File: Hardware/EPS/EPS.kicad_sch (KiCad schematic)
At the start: 0 parts

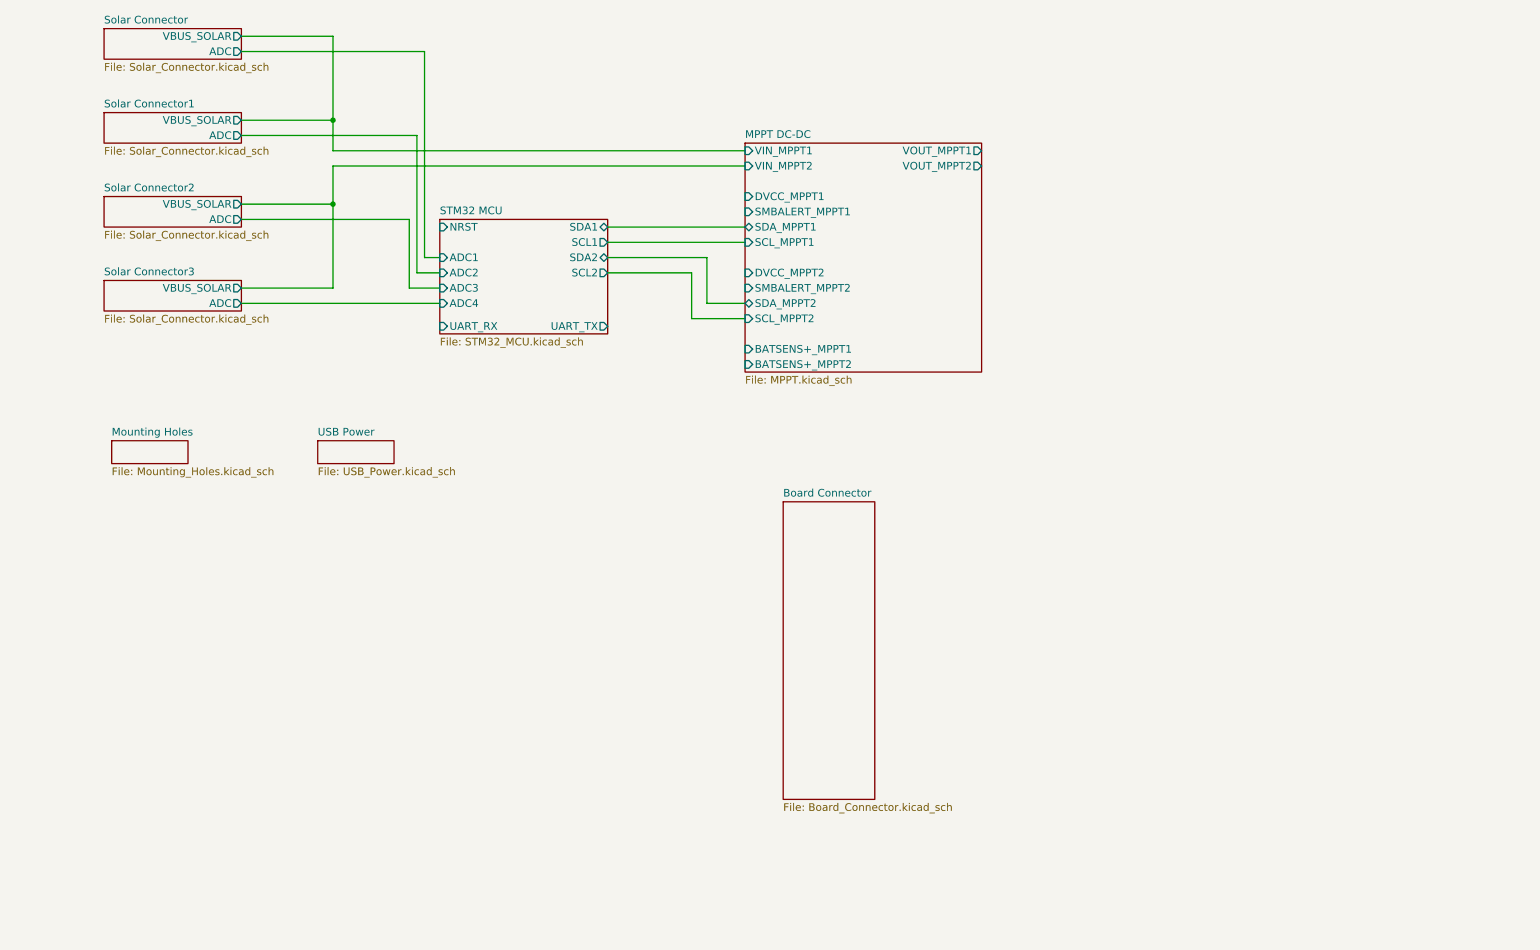
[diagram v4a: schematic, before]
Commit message: Added board connector layout
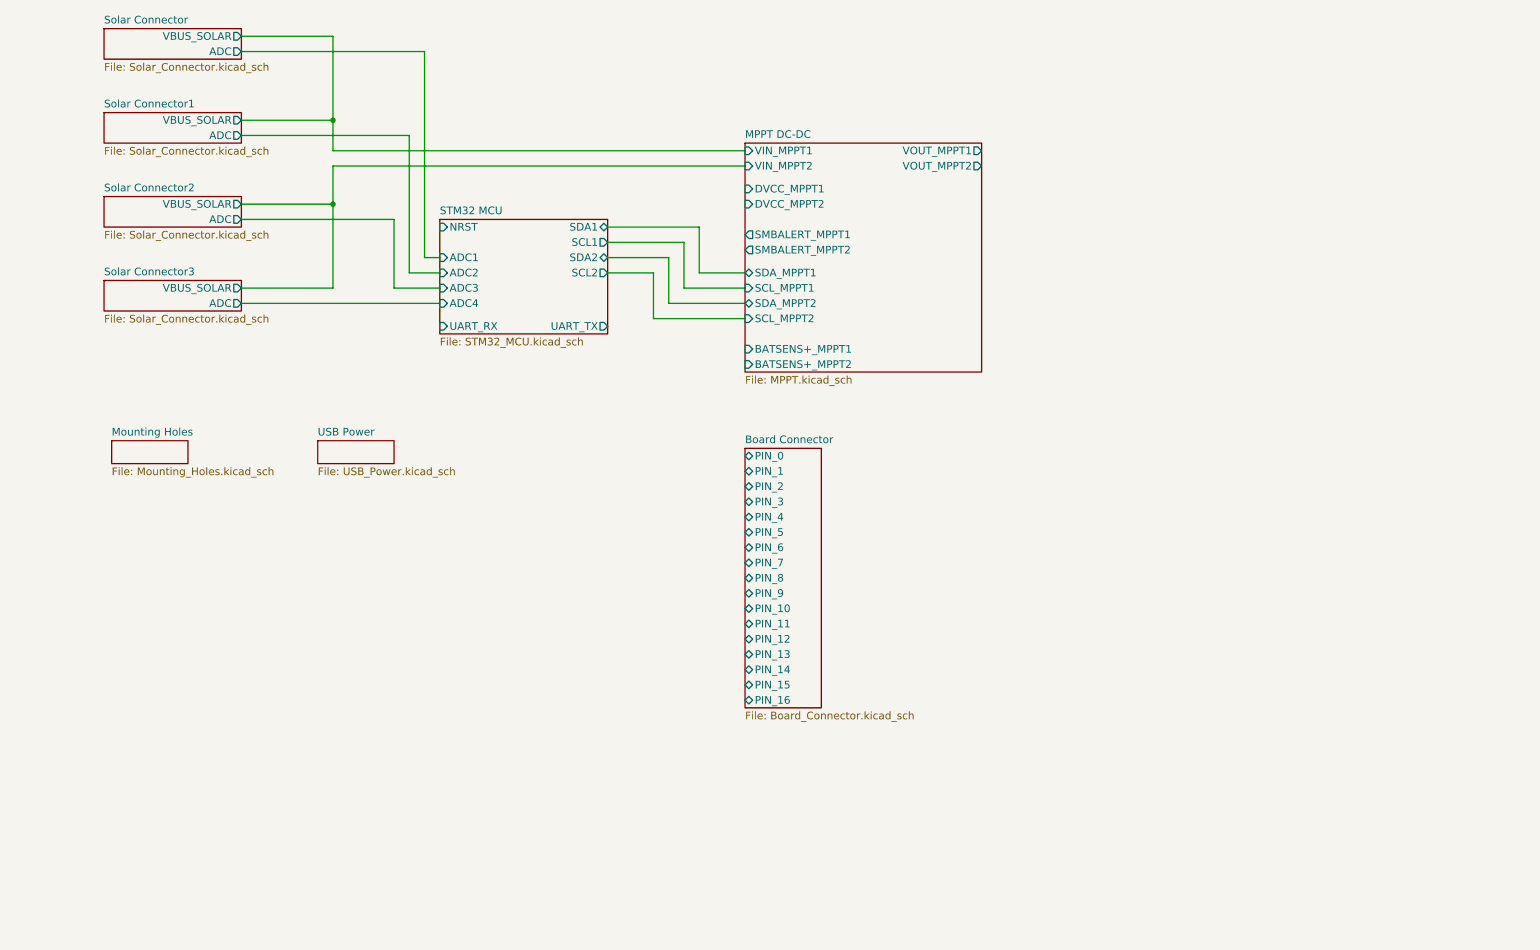
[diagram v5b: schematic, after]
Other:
- sheet Board Connector ports: added PIN_0, PIN_1, PIN_10, PIN_11, PIN_12, PIN_13, PIN_14, PIN_15, PIN_16, PIN_2, PIN_3, PIN_4, PIN_5, PIN_6, PIN_7, PIN_8, PIN_9; removed none

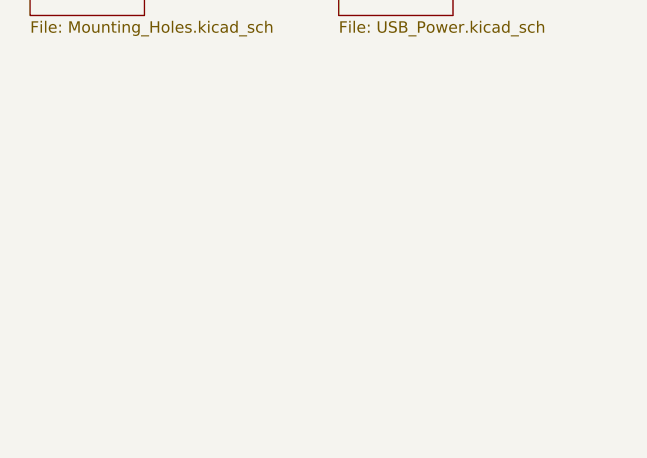
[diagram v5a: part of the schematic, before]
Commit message: Added Power sheet and ESD Protection
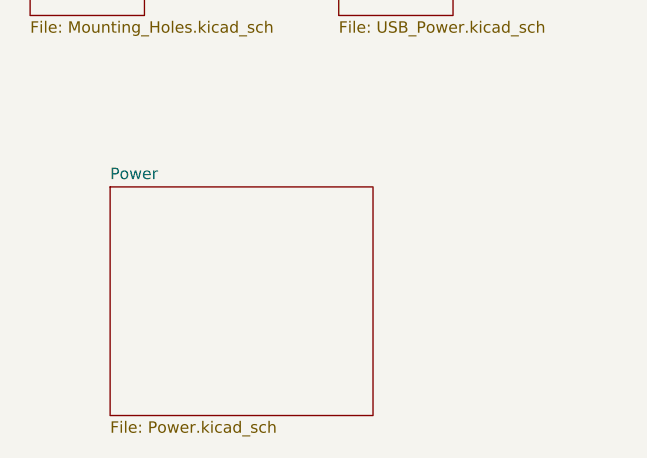
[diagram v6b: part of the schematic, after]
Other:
- added sheet Power (Power.kicad_sch)

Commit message: EPS v0.0.1
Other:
- removed sheet Solar Connector
- removed sheet Solar Connector1
- removed sheet Solar Connector2
- removed sheet Solar Connector3
- added sheet Battery_Connector (Battery_Connector.kicad_sch)
- added sheet Solar_Connector (Solar_Connector.kicad_sch)
- added sheet Solar_Connector1 (Solar_Connector.kicad_sch)
- added sheet Solar_Connector2 (Solar_Connector.kicad_sch)
- added sheet Solar_Connector3 (Solar_Connector.kicad_sch)
- sheet MPPT DC-DC ports: added ~{SMBALERT_MPPT1}; removed BATSENS+_MPPT2, DVCC_MPPT2, SCL_MPPT2, SDA_MPPT2, SMBALERT_MPPT1, SMBALERT_MPPT2, VIN_MPPT2, VOUT_MPPT2
- sheet Power ports: added EN_3V3, EN_5V0, VBUS_IN; removed none
- sheet STM32 MCU ports: added none; removed SCL2, SDA2
- sheet USB Power ports: added USB_VBUS; removed none

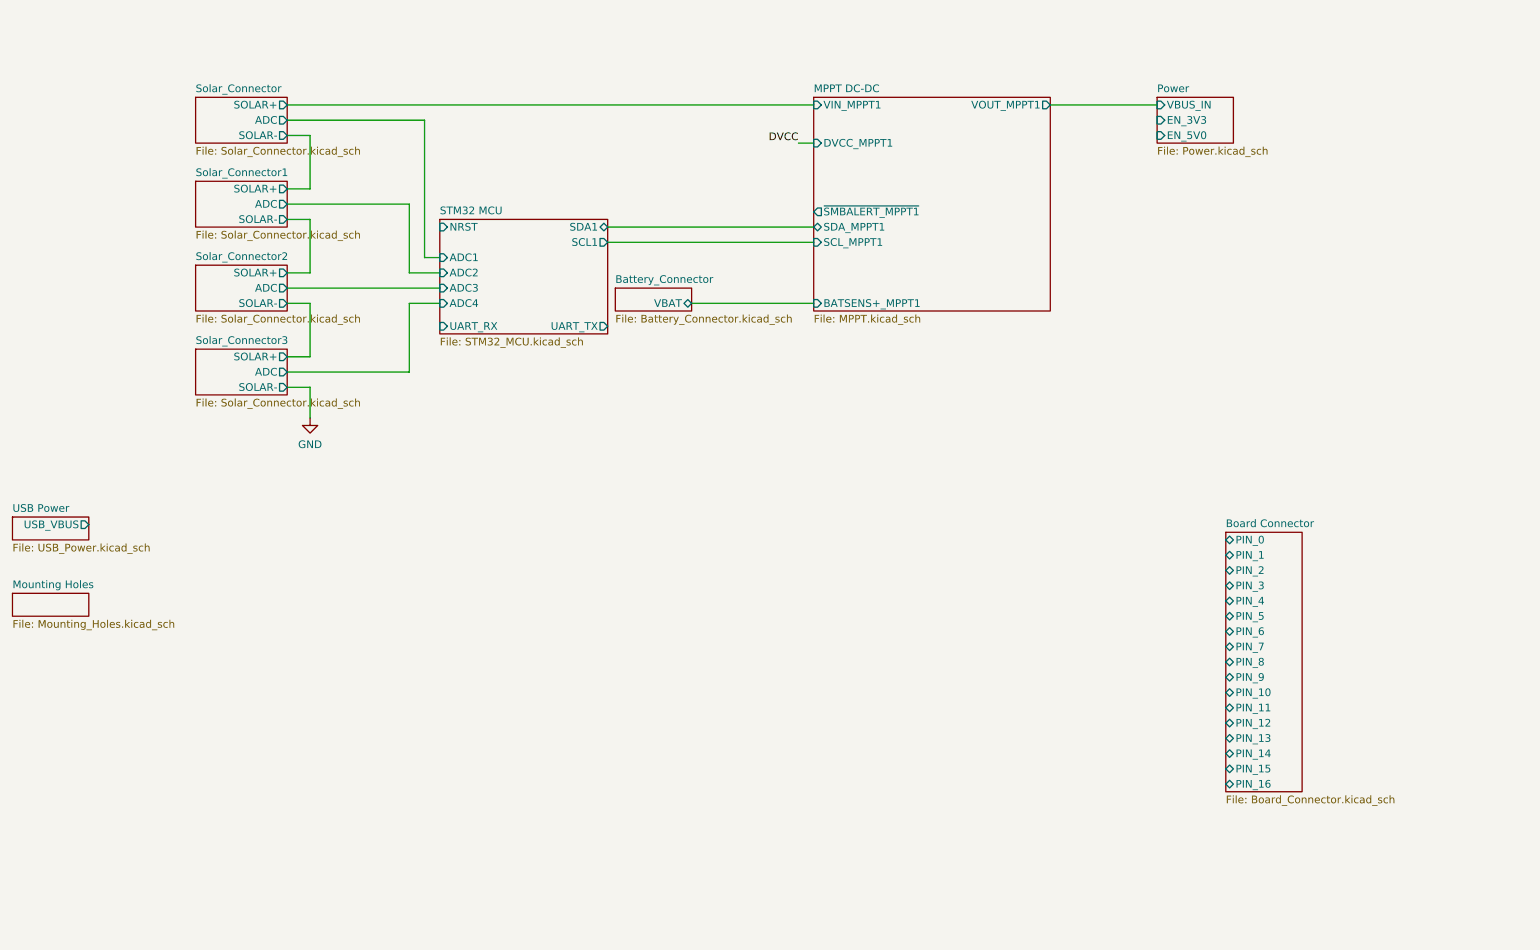
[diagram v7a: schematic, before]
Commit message: Fuse, Power Switch to 3.3V, connector ESD Prot.
v0.0.2
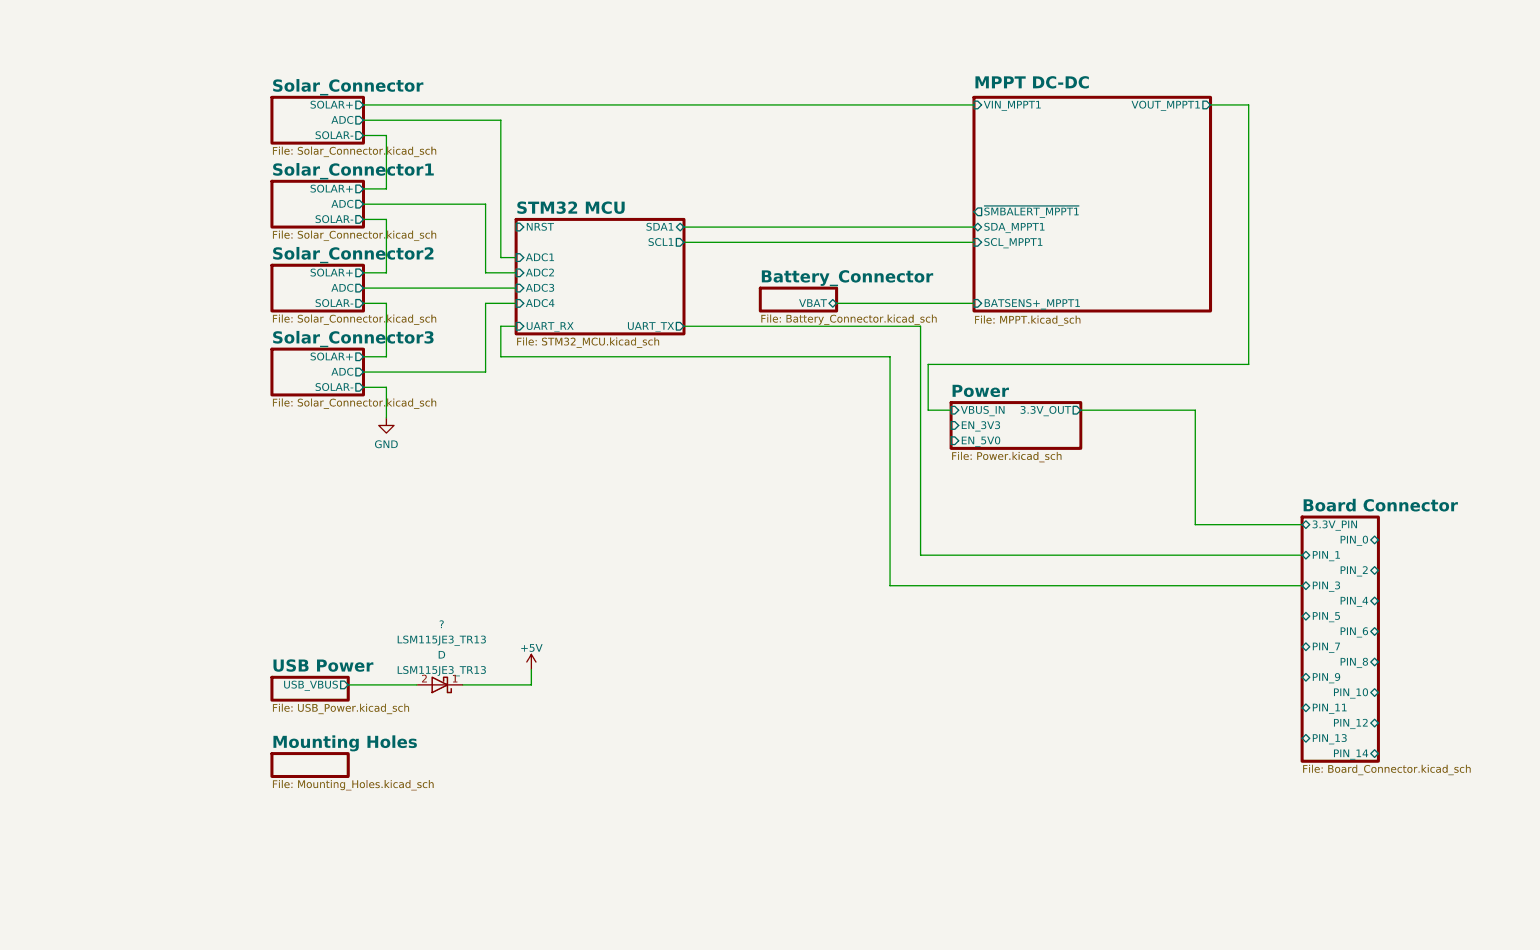
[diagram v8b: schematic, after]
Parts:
- added ?: LSM115JE3_TR13, symbol LSM115JE3_TR13:LSM115JE3_TR13
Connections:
- net USB Power/USB_VBUS: now also ?.2 (A)
- new net +5V: ?.1 (K)
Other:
- sheet Board Connector ports: added 3.3V_PIN; removed PIN_15, PIN_16
- sheet MPPT DC-DC ports: added none; removed DVCC_MPPT1
- sheet Power ports: added 3.3V_OUT; removed none
- title: (none) -> EPS Schematics
